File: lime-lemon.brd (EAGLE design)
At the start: 94 x 88 mm, 96 parts, among them Q1 BSZ105N04NS

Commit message: adds corrections to lime-lemon
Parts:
- removed R51, R59: (no value), rcl:R0805
- CBOOT, CVCC: value (none) -> 100n
- CCOMP3: value (none) -> 300p
- COUT: value (none) -> 22u
- COUTX: value (none) -> 1u
- CRAMP: value (none) -> 180p
- CRST: value (none) -> 22n
- RCOMP2: value (none) -> 7.87k
- RFBT: value (none) -> 36.5k
- RRAMP: value (none) -> 43k
- RSENSE: value (none) -> 0.06
- moved U$1 0.80 mm to (6.00, 37.0)
- renumbered C10 to CBOOT, C11 to CRAMP, C12 to CCOMP3, C14 to CVCC, C16 to CRST, C17 to COUTX, C6 to COUT, C8 to CIO, R49 to RRAMP, R54 to RSENSE, R57 to RFBT, R58 to RCOMP2
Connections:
- removed net N$55: CRST.1, U$2.P$15
- net GND: now also CCOMP3.1, U$2.P$16
- net N$52: now also D2.A, RSENSE.1, U$2.P$13; no longer CRAMP.1, R51.2, RRAMP.2
- net N$53: now also RRAMP.2; no longer R51.1
- net N$57: no longer R59.2
- net N$60: now also CRST.2, U$2.P$15; no longer RSENSE.2, U$2.P$13
- net VDD: now also CRST.1, RSENSE.2; no longer CCOMP3.1, CRST.2, D2.A, R59.1, U$1.P$11, U$2.P$16
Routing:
- net A_HI-LO_OUT: track 106.9 -> 95.0 mm
- net A_LO-HI_IN: track 50.5 -> 40.9 mm
- net A_HI-LO_IN: track 9.90 -> 2.65 mm
- net DIGI_LOW_2: track 20.2 -> 14.3 mm
- net VCC: track 210.8 -> 204.9 mm
- net DIGI_HIGH_1: track 55.7 -> 50.1 mm
- net DIGI_LOW_1: track 55.9 -> 51.6 mm
- net DIGI_HIGH_2: track 23.1 -> 19.9 mm
- net A_LO-HI_OUT: track 118.0 -> 117.4 mm

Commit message: add negative voltage booster to lime-lemon
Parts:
- added CCOMP1: 150p, rcl:C0805
- added R49: 5k6, rcl:R0805
- added RCOMP1: 1k, rcl:R0805
- added RFBT1: 3k3, rcl:R0805
- added RT1: 220, rcl:R0805
- added RUV3: 270, rcl:R0805
- CCOMP3: value 300p -> 150p
- R55: value 226k -> 220k
- RCOMP2: value 7.87k -> 6.8k
- RFBT: value 36.5k -> 33k
- RT: value 10.2k -> 10k
- RUV1: value 3.57k -> 3.3k
- moved Q1 258.0 mm to (54.0, 78.0), turned to 90 degrees
- moved CRST 255.5 mm to (50.0, 68.0), turned to 270 degrees
- moved RFPP2 255.2 mm to (39.0, 67.0), turned to 90 degrees
- moved D2 254.0 mm to (58.0, 71.0), turned to 270 degrees
- moved U$3 244.2 mm to (63.0, 65.0), turned to 90 degrees
- moved RUV2 232.4 mm to (13.0, 81.0), turned to 180 degrees
- moved RCOMP2 225.3 mm to (59.0, 54.0)
- moved RSENSE 224.2 mm to (50.0, 72.0), turned to 270 degrees
- moved RFBT 223.6 mm to (54.0, 58.0), turned to 90 degrees
- moved RUV1 220.1 mm to (17.0, 80.0), turned to 90 degrees
- moved R55 218.8 mm to (30.0, 68.0)
- moved RT 208.7 mm to (43.0, 66.0)
- moved RRAMP 208.6 mm to (32.0, 81.0)
- moved RFBB1 205.0 mm to (40.0, 71.0)
- moved CCOMP2 193.0 mm to (35.0, 68.0)
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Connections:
- new net N$55: RUV1.1, RUV3.2
- new net N$66: R49.2, R55.1
- new net N$72: RT1.1, U$2.P$5
- new net N$73: RCOMP1.1, RCOMP2.1
- new net N$74: RFBT.1, RFBT1.2
- net GND: now also BOOST.7, CCOMP1.1, RFBT.2
- net N$53: now also CRAMP.1
- net N$54: now also RT1.2; no longer U$2.P$5
- net N$56: now also R49.1; no longer R55.1
- net N$57: now also RCOMP1.2, RFBT1.1; no longer RCOMP2.1, RFBT.1
- net N$71: now also CCOMP1.2
- net VDD: now also RUV3.1; no longer RUV1.1
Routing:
- net VDD: track 118.6 -> 314.4 mm, vias 3 -> 2
- net +5V: track 0.00 -> 96.0 mm, vias 0 -> 3
- net GND: track 27.2 -> 92.3 mm
- net N$57: track 0.00 -> 45.2 mm
- net N$65: track 0.00 -> 35.6 mm
- net N$43: track 0.00 -> 35.3 mm
- net N$58: track 0.00 -> 31.9 mm
- net N$61: track 0.00 -> 30.1 mm
- net N$48: track 0.00 -> 24.4 mm, vias 0 -> 2
- net N$45: track 0.00 -> 19.2 mm
- net N$52: track 0.00 -> 18.1 mm
- net N$60: track 0.00 -> 13.3 mm
- net A_LO-HI_OUT: track 117.4 -> 129.1 mm, vias 0 -> 1
- net A_HI-LO_OUT: track 95.0 -> 106.6 mm
- net N$9: track 84.5 -> 73.0 mm
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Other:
- board size 94 x 88 mm -> 94 x 121 mm
- board text added: "Protopaja 13.7.2016 UADIVOLECO "Lime-Lemon""
- board text removed: "Protopaja 5.7.2016 UADIVOLECO "Appelsiini""

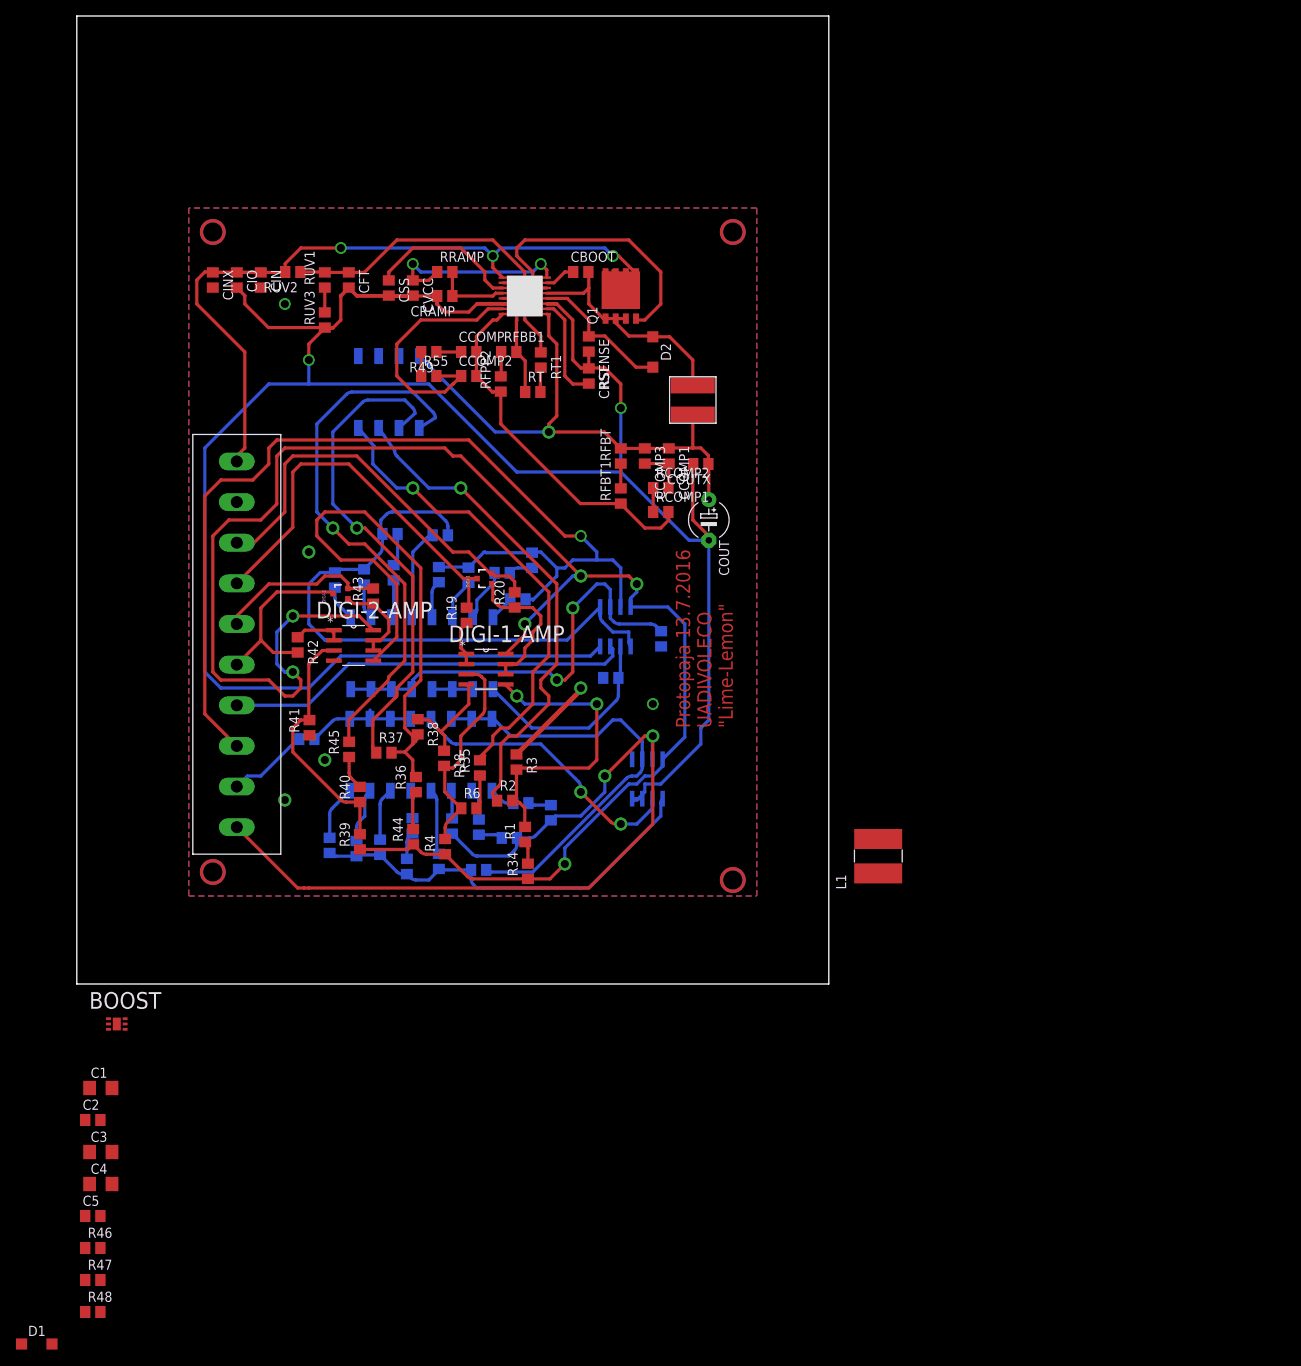
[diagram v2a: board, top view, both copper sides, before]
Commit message: Finishes the lime-lemon board
makes the lime-lemon board complete and ready for manufacturing
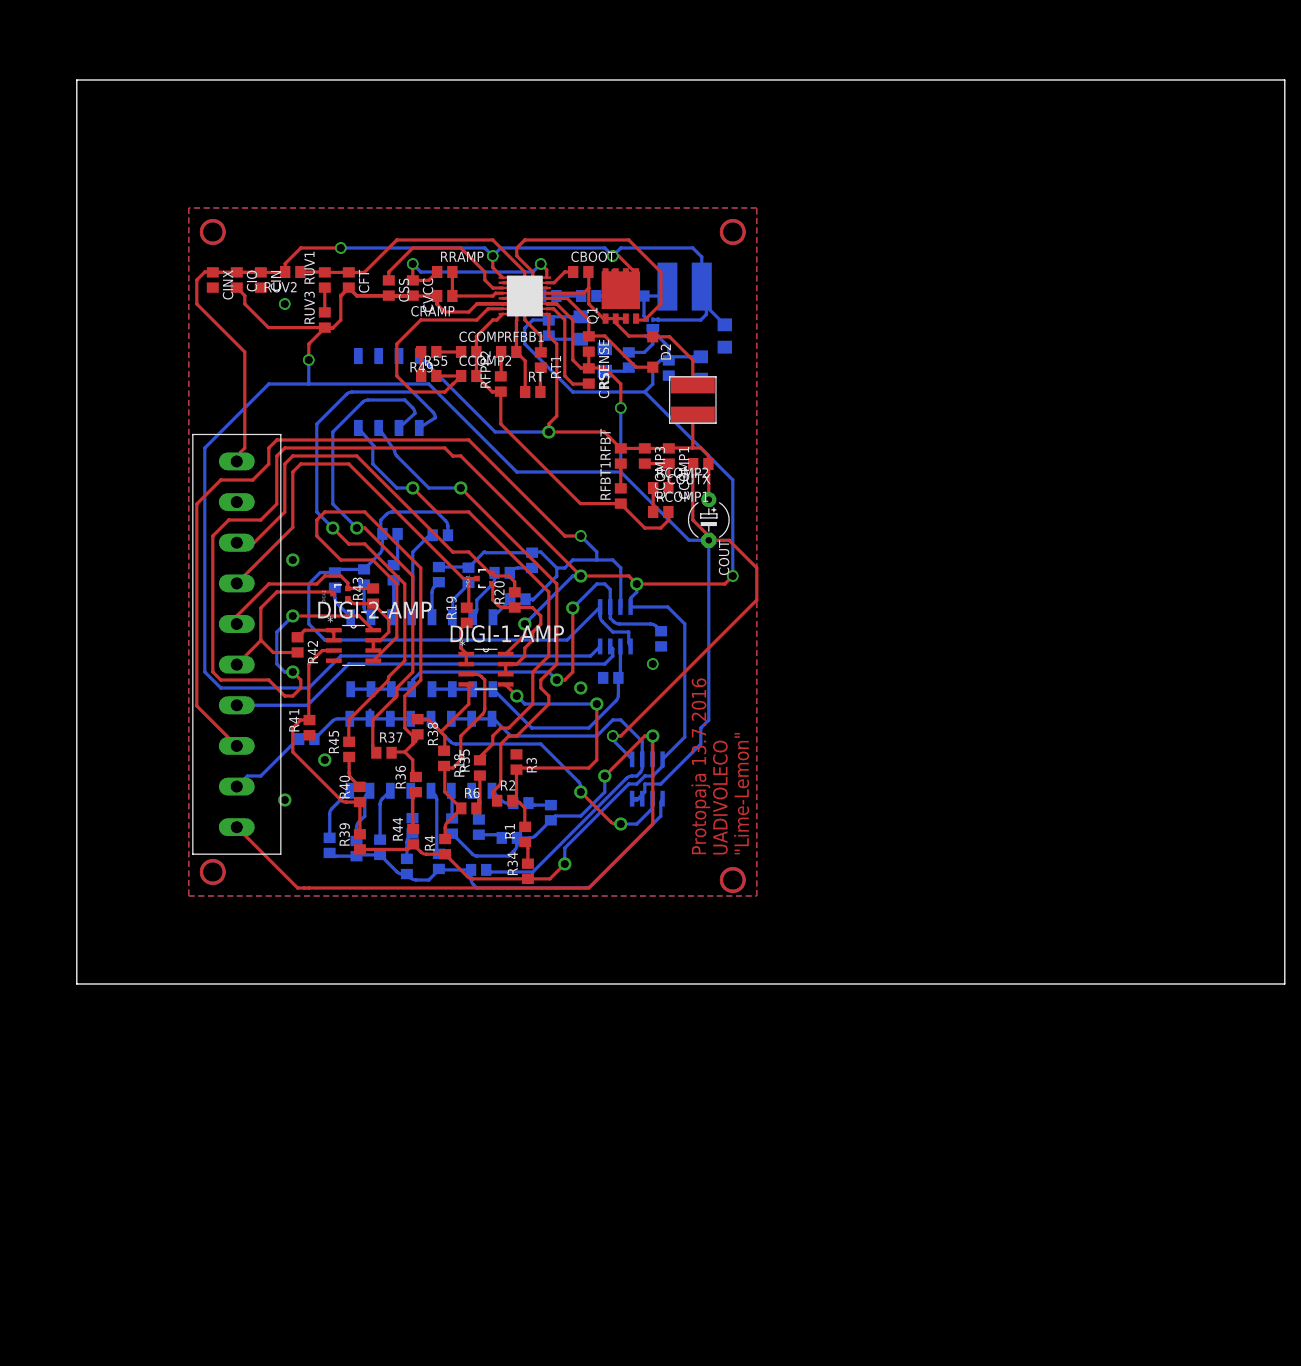
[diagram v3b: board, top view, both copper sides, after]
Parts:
- added R50: (no value), rcl:R0805
- C5: device rcl:C0805 -> rcl:C1206
- moved D1 150.5 mm to (55.0, 78.0), flipped to the bottom, turned to 180 degrees
- moved R48 136.6 mm to (55.0, 70.0), flipped to the bottom, turned to 90 degrees
- moved R47 135.6 mm to (45.0, 78.0), flipped to the bottom, turned to 180 degrees
- moved R46 128.4 mm to (45.0, 74.0), flipped to the bottom, turned to 270 degrees
- moved C5 124.7 mm to (52.0, 70.0), flipped to the bottom, turned to 90 degrees
- moved C3 123.4 mm to (64.0, 69.0), flipped to the bottom, turned to 270 degrees
- moved C4 122.7 mm to (49.0, 74.0), flipped to the bottom, turned to 270 degrees
- moved C1 122.1 mm to (67.0, 73.0), flipped to the bottom, turned to 270 degrees
- moved C2 118.4 mm to (60.0, 69.0), flipped to the bottom, turned to 270 degrees
- moved BOOST 109.8 mm to (58.0, 74.0), flipped to the bottom, turned to 90 degrees
- moved L1 74.9 mm to (62.0, 79.0), flipped to the bottom, turned to 180 degrees
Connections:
- new net N$75: D1.C, R50.2
- net +5V: now also C1.1; no longer C2.1
- net N$47: now also R50.1; no longer D1.C
- net VCC: now also C2.1; no longer C1.1
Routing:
- net VCC: track 211.8 -> 295.9 mm, vias 6 -> 7
- net VDD: track 314.4 -> 354.8 mm, vias 2 -> 3
- net +5V: track 96.0 -> 125.7 mm
- net N$44: track 0.00 -> 6.55 mm
- net N$49: track 0.00 -> 4.39 mm
- net N$51: track 0.00 -> 3.19 mm
- net N$47: track 0.00 -> 3.10 mm
- net GND: track 92.3 -> 89.4 mm
- net N$75: track 0.00 -> 2.15 mm
- net A_LO-HI_OUT: track 129.1 -> 129.9 mm
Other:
- board size 94 x 121 mm -> 151 x 113 mm
